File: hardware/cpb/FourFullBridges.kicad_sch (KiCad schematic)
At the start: 31 parts, among them Q5 PMBT2222A, Q6 IRF9393, Q7 PMBT2222A, U7 SC18IS606, U8 KF33BDT, U9 MAX22200

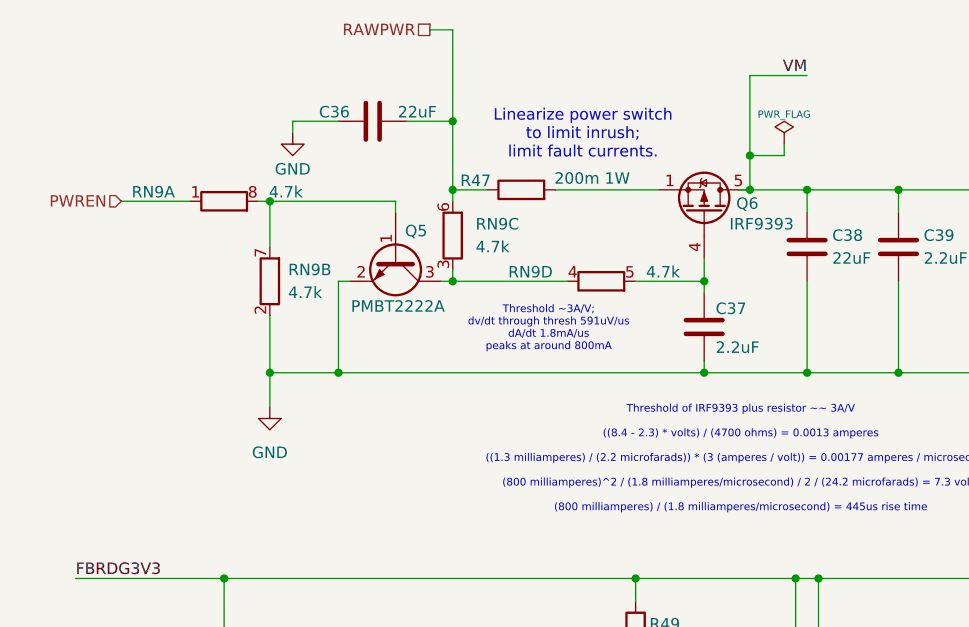
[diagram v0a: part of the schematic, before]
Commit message: hardware/cpb: RN vias and 2.2 nF capacitor fixed.
Vias on all RNs are now have a proper fanout and C37 was moved and now connects between the gate and VBATT+.
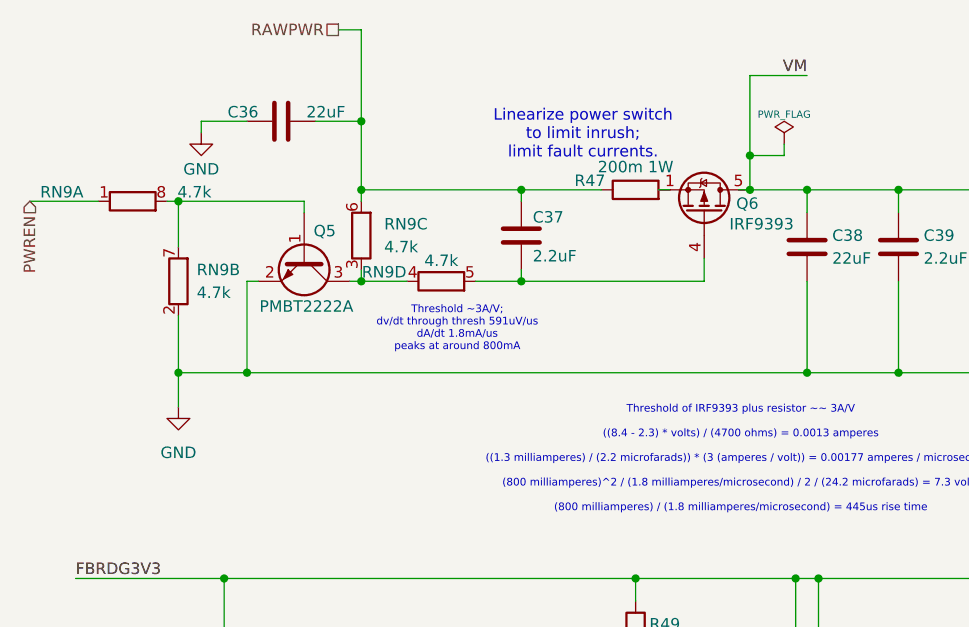
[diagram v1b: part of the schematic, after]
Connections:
- net GND: no longer C37.2
- net RAWPWR: now also C37.1
- net at Q6.4 (G), RN9.5 (R4.2): now also C37.2; no longer C37.1
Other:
- moved on the sheet: C36, C37, Q5, R47, RN9A, RN9B, RN9C, RN9D

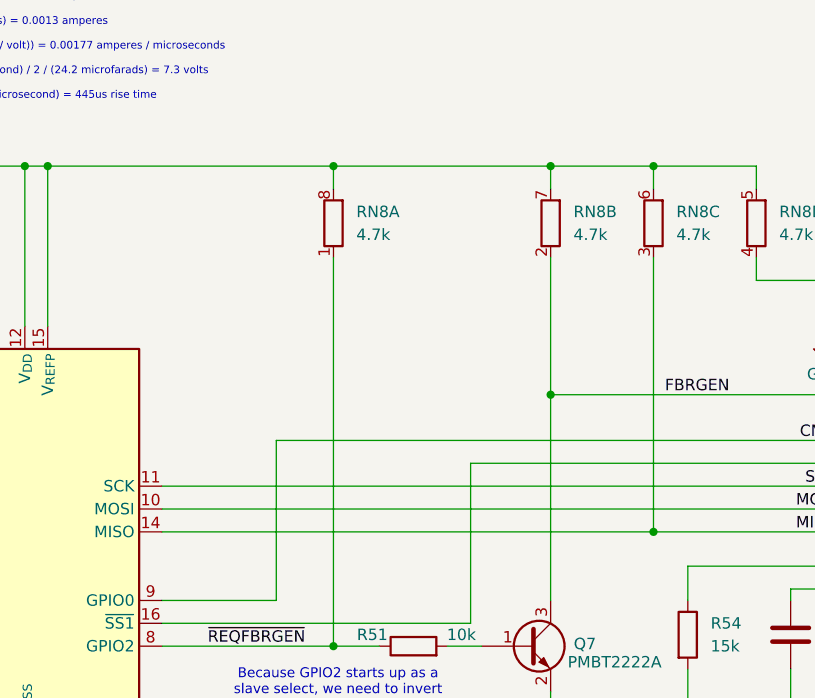
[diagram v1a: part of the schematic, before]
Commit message: hardware/cpb: r96 changed to  3.3k and r46 added
R96 changed resistance from 10k to 3.3k, r46 added from 3.3v to Max22200(1k resistance)
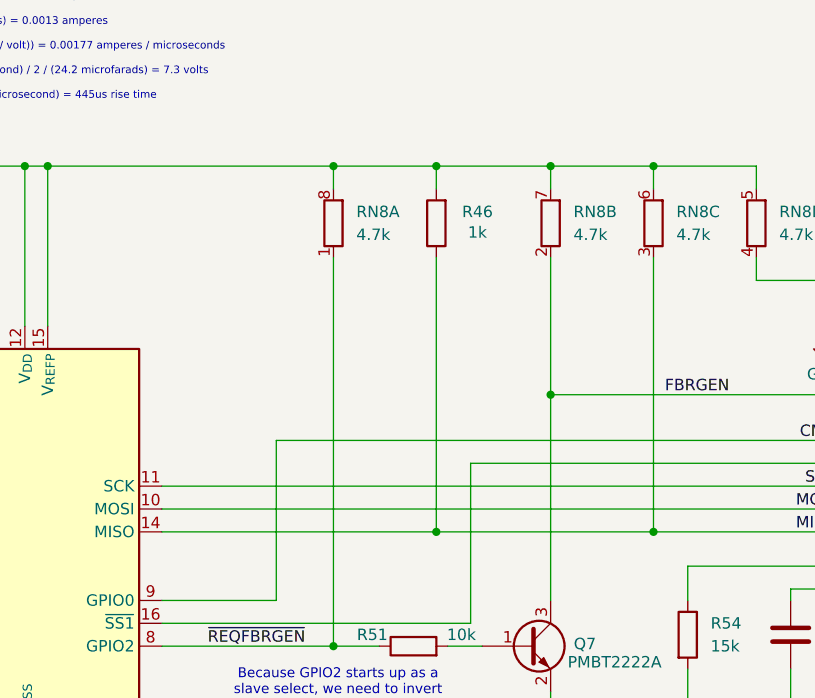
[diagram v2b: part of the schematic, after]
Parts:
- added R46: 1k, Resistor_SMD:R_0603_1608Metric, symbol Device:R
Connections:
- net FBRDG3V3: now also R46.2
- net MISO: now also R46.1
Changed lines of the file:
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@@
 	)
 	(junction
+		(at 144.78 93.98)
+		(diameter 0)
+		(color 0 0 0 0)
+	)
+	(junction
 		(at 99.06 93.98)
 		(diameter 0)
@@
 	)
 	(junction
+		(at 144.78 134.62)
+		(diameter 0)
+		(color 0 0 0 0)
+	)
+	(junction
 		(at 147.32 71.12)
 		(diameter 0)
@@
 	(wire
 		(pts
-			(xy 114.3 134.62) (xy 168.91 134.62)
+			(xy 114.3 134.62) (xy 144.78 134.62)
 		)
 		(stroke
@@
 	(wire
 		(pts
+			(xy 127 124.46) (xy 191.77 124.46)
+		)
+		(stroke
+			(width 0)
+			(type default)
+		)
+	)
+	(wire
+		(pts
 			(xy 76.2 147.32) (xy 76.2 158.75)
 		)
@@
 	(wire
 		(pts
-			(xy 127 124.46) (xy 191.77 124.46)
+			(xy 144.78 93.98) (xy 157.48 93.98)
 		)
 		(stroke
@@
 	(wire
 		(pts
+			(xy 144.78 93.98) (xy 144.78 96.52)
+		)
+		(stroke
+			(width 0)
+			(type default)
+		)
+	)
+	(wire
+		(pts
 			(xy 45.72 43.18) (xy 50.8 43.18)
 		)
@@
 	(wire
 		(pts
+			(xy 144.78 134.62) (xy 168.91 134.62)
+		)
+		(stroke
+			(width 0)
+			(type default)
+		)
+	)
+	(wire
+		(pts
 			(xy 204.47 71.12) (xy 194.31 71.12)
 		)
@@
 	(wire
 		(pts
+			(xy 144.78 104.14) (xy 144.78 134.62)
+		)
+		(stroke
+			(width 0)
+			(type default)
+		)
+	)
+	(wire
+		(pts
 			(xy 236.22 90.17) (xy 236.22 95.25)
 		)
@@
 	(wire
 		(pts
-			(xy 133.35 93.98) (xy 157.48 93.98)
+			(xy 133.35 93.98) (xy 144.78 93.98)
 		)
 		(stroke
@@
 					(unit 1)
 				)
+			)
+		)
+	)
+	(symbol
+		(lib_id "Device:R")
+		(at 144.78 100.33 180)
+		(unit 1)
+		(exclude_from_sim no)
+		(in_bom yes)
+		(on_board yes)
+		(dnp no)
+		(property "Reference" "R46"
+			(at 149.352 99.06 0)
+			(effects
+				(font
+					(size 1.27 1.27)
+				)
+			)
+		)
+		(property "Value" "1k"
+			(at 149.352 101.346 0)
+			(effects
+				(font
+					(size 1.27 1.27)
+				)
+			)
+		)
+		(property "Footprint" "Resistor_SMD:R_0603_1608Metric"
+			(at 146.558 100.33 90)
+			(effects
+				(font
+					(size 1.27 1.27)
+				)
+				(hide yes)
+			)
+		)
+		(property "Datasheet" "~"
+			(at 144.78 100.33 0)
+			(effects
+				(font
+					(size 1.27 1.27)
+				)
+				(hide yes)
+			)
+		)
+		(property "Description" "Resistor"
+			(at 144.78 100.33 0)
+			(effects
+				(font
+					(size 1.27 1.27)
+				)
+				(hide yes)
+			)
+		)
+		(property "LCSC" "C22548"
+			(at 144.78 100.33 0)
+			(effects
+				(font
+					(size 1.27 1.27)
+				)
+				(hide yes)
+			)
+		)
+		(pin "2"
+		)
+		(pin "1"
+		)
+		(instances
+			(project "cpb"
+				(path "/9a10a1ee-db5a-47ad-90f3-81b92d74d449/1d0e9b27-ccf6-43da-9db7-61f18e9cbbee"
+					(reference "R46")
+					(unit 1)
+				)

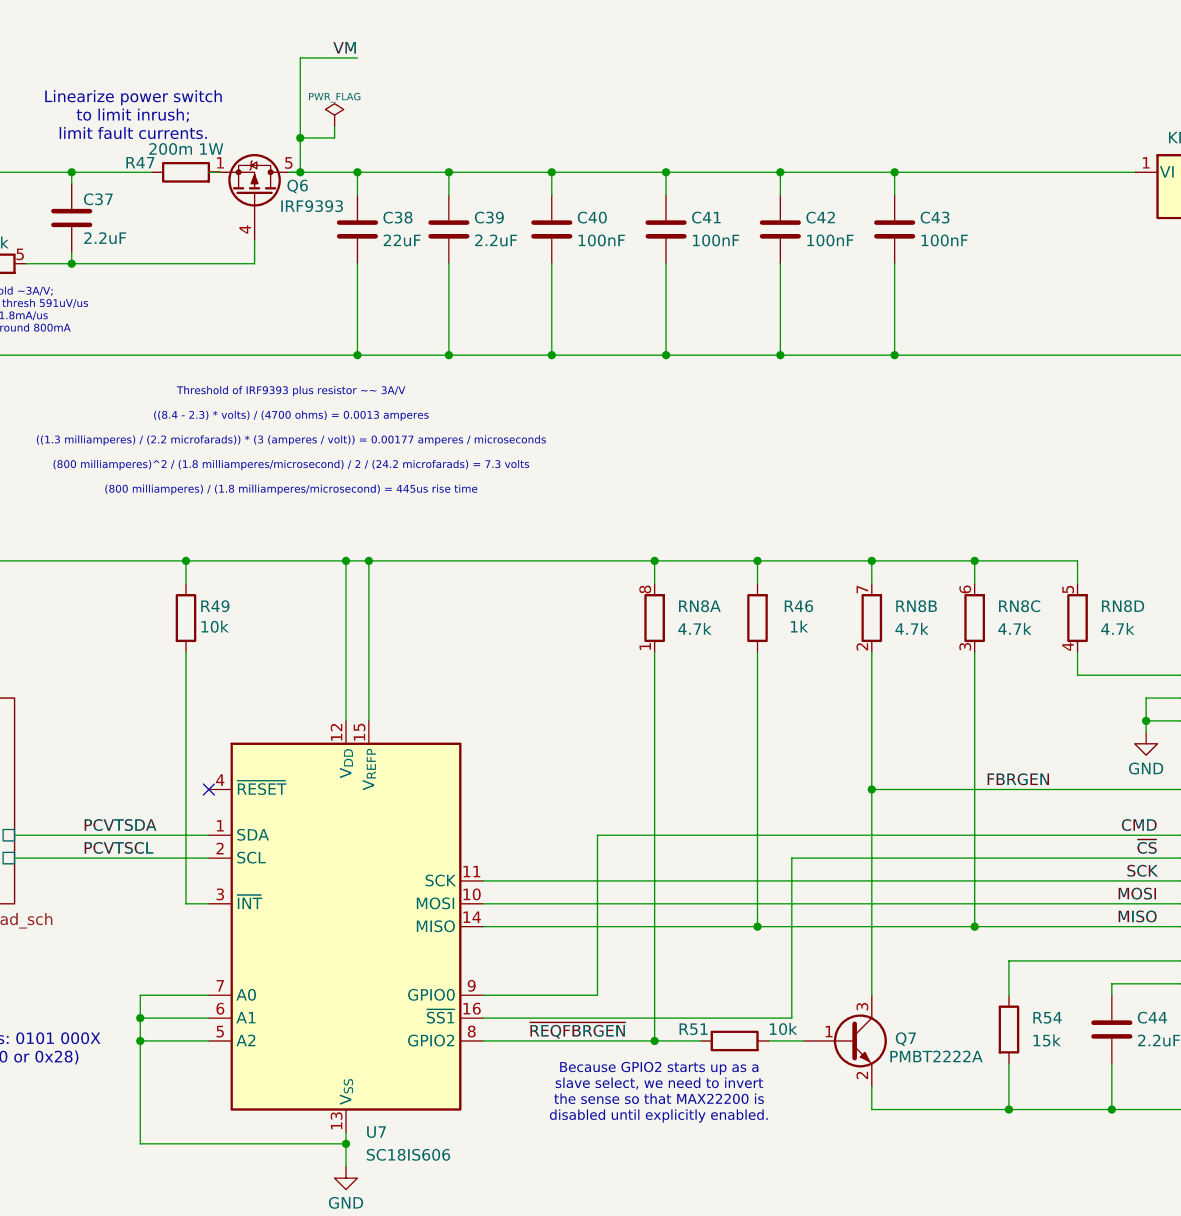
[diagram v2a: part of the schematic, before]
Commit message: hardware/cpb: changed from european to american symbols.
RN parts still are european for now. Changed via TextEdit replace all tool. Device:R --> Device:R_US
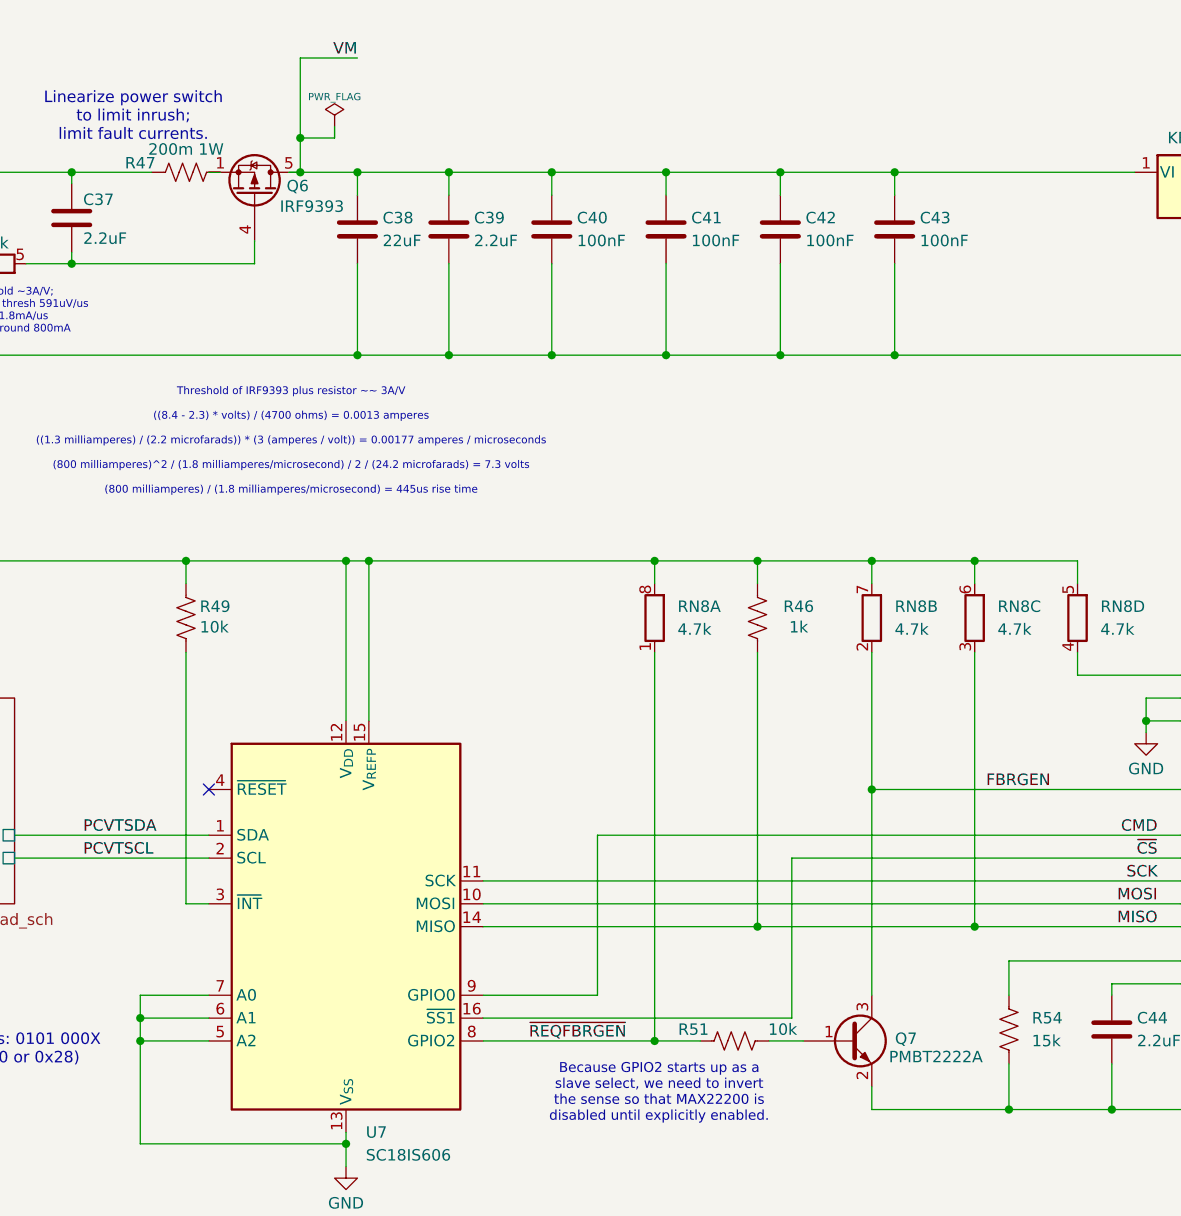
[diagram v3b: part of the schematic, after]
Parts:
- R46, R47, R49, R51, R54: symbol Device:R -> Device:R_US
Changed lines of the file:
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@@
 	)
 	(symbol
-		(lib_id "Device:R")
+		(lib_id "Device:R_US")
 		(at 172.72 146.05 0)
 		(unit 1)
@@
 	)
 	(symbol
-		(lib_id "Device:R")
+		(lib_id "Device:R_US")
 		(at 144.78 100.33 180)
 		(unit 1)
@@
 	)
 	(symbol
-		(lib_id "Device:R")
+		(lib_id "Device:R_US")
 		(at 142.24 147.32 90)
 		(unit 1)
@@
 	)
 	(symbol
-		(lib_id "Device:R")
+		(lib_id "Device:R_US")
 		(at 81.28 50.8 90)
 		(unit 1)
@@
 	)
 	(symbol
-		(lib_id "Device:R")
+		(lib_id "Device:R_US")
 		(at 81.28 100.33 0)
 		(unit 1)
